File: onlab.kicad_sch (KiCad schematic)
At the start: 77 parts, among them J1 Battery, J10 DC-Motor, J2 HC_SR04, J3 HC_SR04, J4 HC_SR04, J5 DC-Motor, J6 DC-Motor, J7 DC-Motor, J8 DC-Motor, J9 DC-Motor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

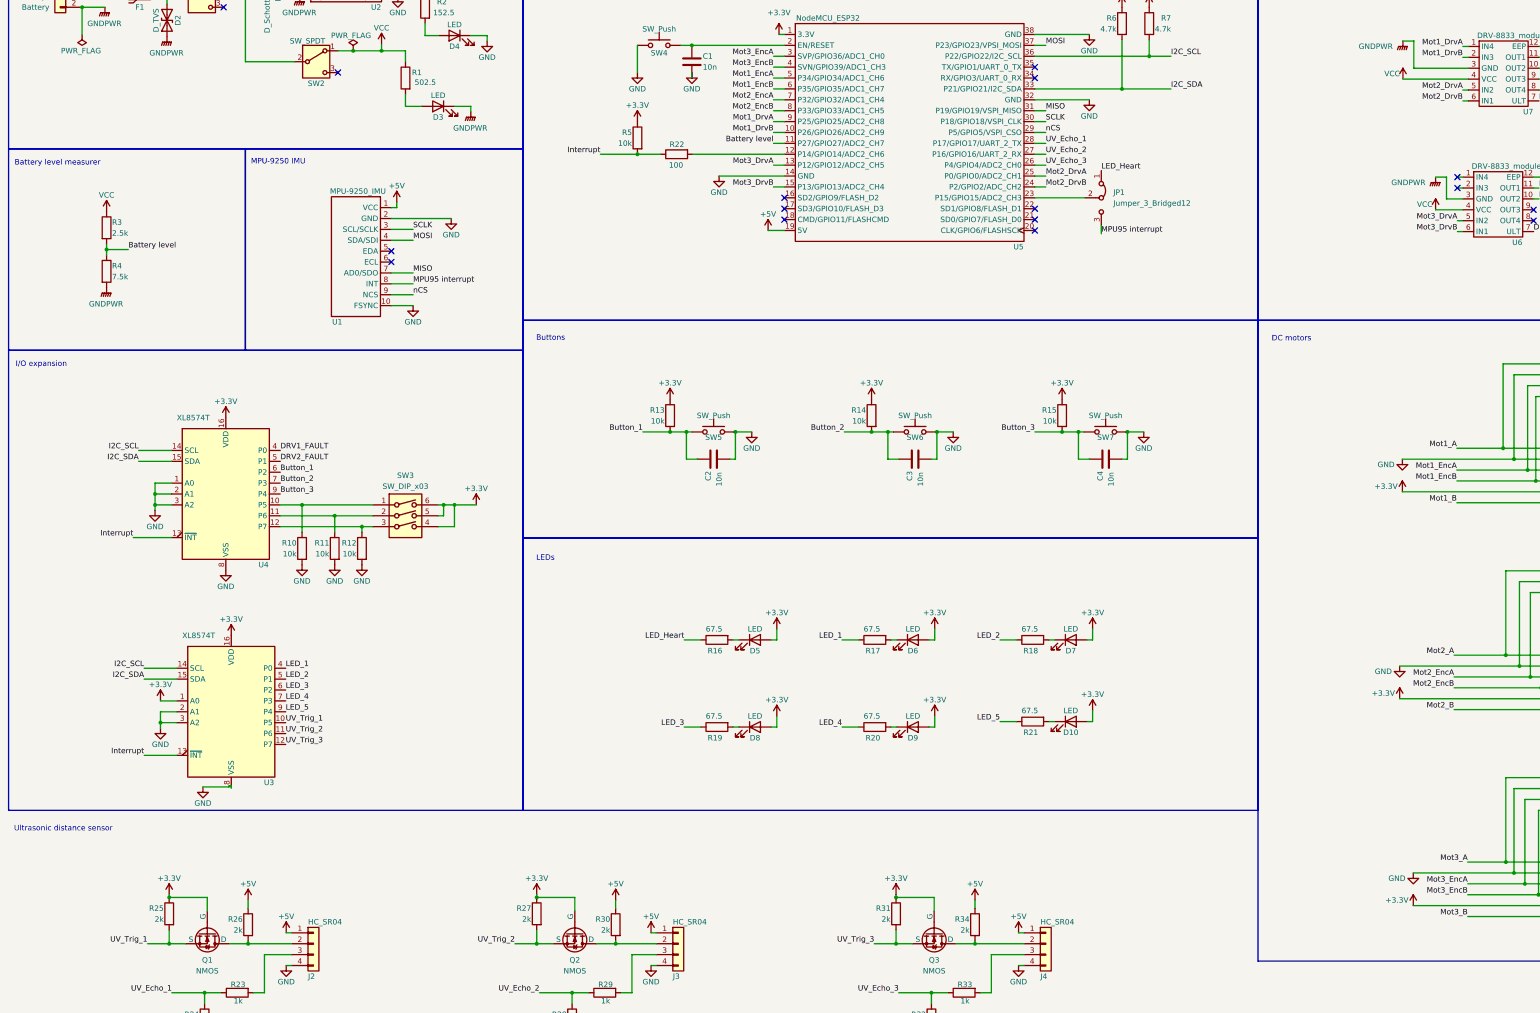
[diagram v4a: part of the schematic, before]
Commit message: schematic update
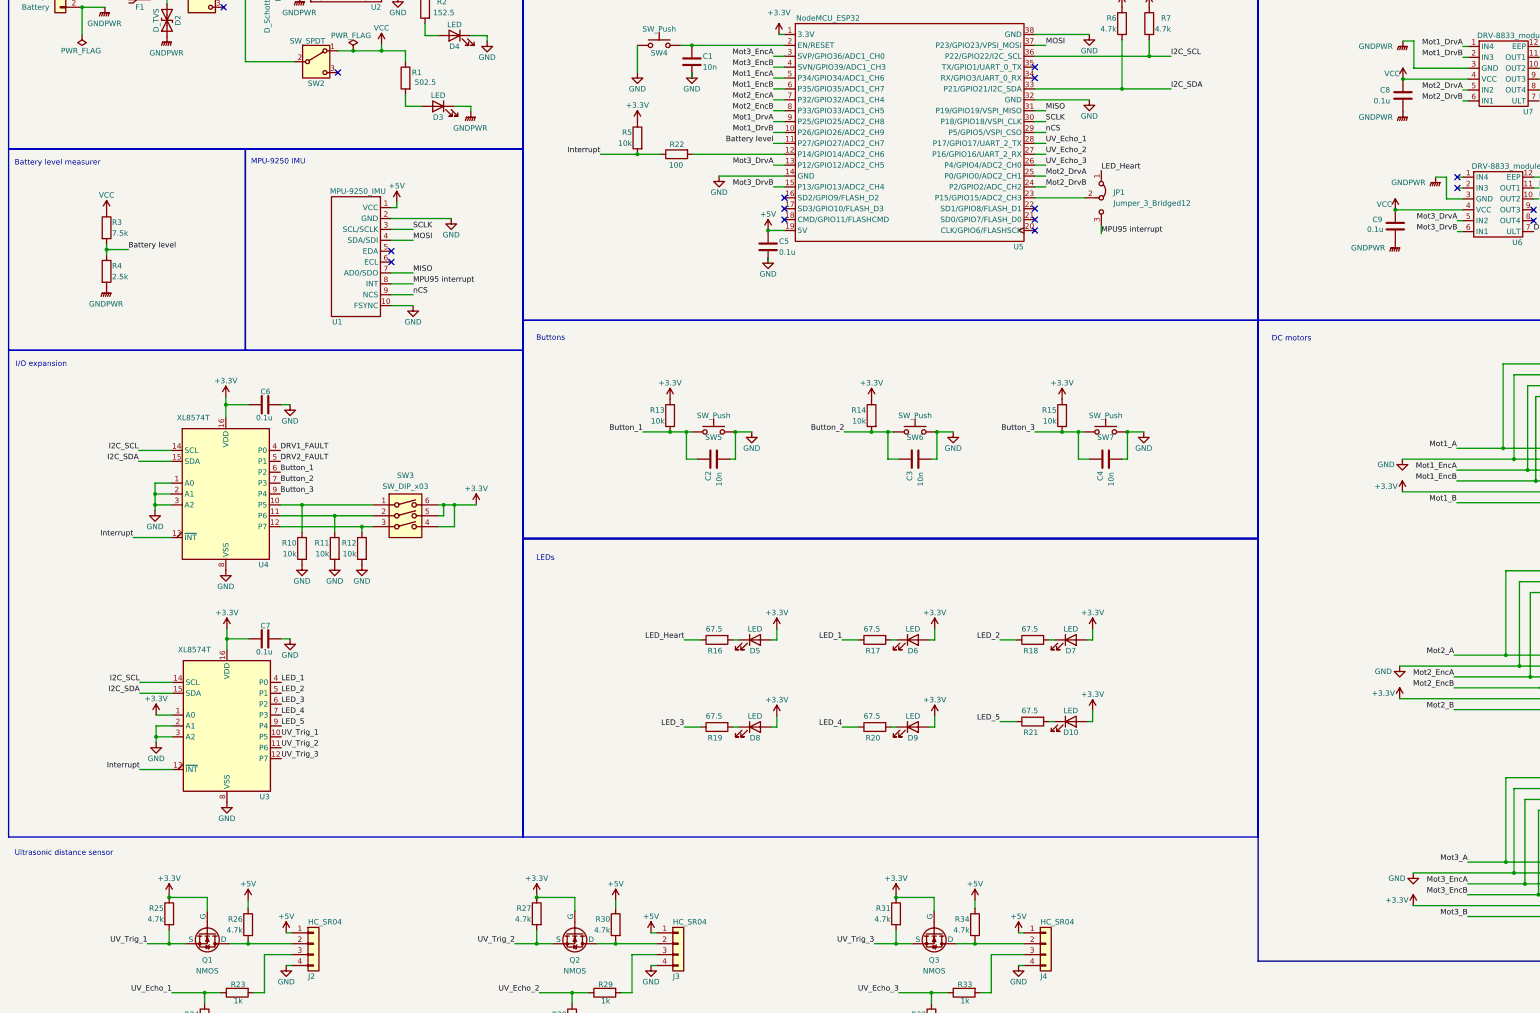
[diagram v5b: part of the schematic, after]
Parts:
- added C5, C6, C7, C8, C9: 0.1u, Capacitor_SMD:C_0805_2012Metric_Pad1.18x1.45mm_HandSolder, symbol Device:C
- R25, R26, R27, R30, R31, R34: value 2k -> 4.7k
- R3: value 2.5k -> 7.5k
- R4: value 7.5k -> 2.5k
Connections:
- net +3.3V: now also C6.1, C7.1
- net +5V: now also C5.1
- net GND: now also C5.2, C6.2, C7.2
- net GNDPWR: now also C8.2, C9.2
- net VCC: now also C8.1, C9.1
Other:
- moved on the sheet: U3

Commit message: footprint assignment final
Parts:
- JP1, SW1, SW2: footprint (none) -> Connector:FanPinHeader_1x03_P2.54mm_Vertical
- Q1, Q2, Q3: footprint (none) -> Package_TO_SOT_SMD:SOT-23_Handsoldering
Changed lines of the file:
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@@
   (title_block
     (title "Robot Schematic")
-    (date "2024-04-23")
-    (rev "v1.0")
+    (date "2024-05-25")
+    (rev "V6.0")
+    (comment 1 "Irányítás Technika Tanszék")
+    (comment 2 "Neptun: QVFLJH")
+    (comment 3 "Made by: Técsi Zsuzsanna Vilma")
   )
   (junction (at 361.315 181.61) (diameter 0) (color 0 0 0 0)
@@
       (effects (font (size 1.27 1.27)))
     )
-    (property "Footprint" "" (at 57.15 27.94 0)
+    (property "Footprint" "Connector:FanPinHeader_1x03_P2.54mm_Vertical" (at 57.15 27.94 0)
       (effects (font (size 1.27 1.27)) hide)
     )
@@
       (effects (font (size 1.27 1.27)))
     )
-    (property "Footprint" "" (at 230.505 251.46 0)
+    (property "Footprint" "Package_TO_SOT_SMD:SOT-23_Handsoldering" (at 230.505 251.46 0)
       (effects (font (size 1.27 1.27)) hide)
     )
@@
       (effects (font (size 1.27 1.27)))
     )
-    (property "Footprint" "" (at 60.96 251.46 0)
+    (property "Footprint" "Package_TO_SOT_SMD:SOT-23_Handsoldering" (at 60.96 251.46 0)
       (effects (font (size 1.27 1.27)) hide)
     )
@@
       (effects (font (size 1.27 1.27)) (justify left))
     )
-    (property "Footprint" "" (at 266.954 74.93 0)
+    (property "Footprint" "Connector:FanPinHeader_1x03_P2.54mm_Vertical" (at 266.954 74.93 0)
       (effects (font (size 1.27 1.27)) hide)
     )
@@
       (effects (font (size 1.27 1.27)))
     )
-    (property "Footprint" "" (at 83.82 43.18 0)
+    (property "Footprint" "Connector:FanPinHeader_1x03_P2.54mm_Vertical" (at 83.82 43.18 0)
       (effects (font (size 1.27 1.27)) hide)
     )
@@
       (effects (font (size 1.27 1.27)))
     )
-    (property "Footprint" "" (at 146.685 251.46 0)
+    (property "Footprint" "Package_TO_SOT_SMD:SOT-23_Handsoldering" (at 146.685 251.46 0)
       (effects (font (size 1.27 1.27)) hide)
     )

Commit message: motor footprint update
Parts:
- J10, J8, J9: footprint Connector_Molex:Molex_KK-254_AE-6410-06A_1x06_P2.54mm_Vertical -> Onlab:motor
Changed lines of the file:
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@@
     (stroke (width 0) (type default))
   )
+  (wire (pts (xy 266.954 67.31) (xy 266.954 68.58))
+    (stroke (width 0) (type default))
+  )
   (wire (pts (xy 104.648 40.64) (xy 99.06 40.64))
     (stroke (width 0) (type default))
@@
     (stroke (width 0) (type default))
   )
+  (wire (pts (xy 267.208 66.294) (xy 267.208 67.31))
+    (stroke (width 0) (type default))
+  )
   (wire (pts (xy 251.46 59.69) (xy 254 59.69))
     (stroke (width 0) (type default))
@@
     (stroke (width 0) (type default))
   )
+  (wire (pts (xy 369.57 82.804) (xy 367.792 82.804))
+    (stroke (width 0) (type default))
+  )
   (wire (pts (xy 50.038 141.478) (xy 46.228 141.478))
     (stroke (width 0) (type default))
@@
     (stroke (width 0) (type default))
   )
+  (wire (pts (xy 267.208 67.31) (xy 266.954 67.31))
+    (stroke (width 0) (type default))
+  )
   (wire (pts (xy 80.518 146.558) (xy 80.518 152.908))
     (stroke (width 0) (type default))
@@
     (stroke (width 0) (type default))
   )
+  (wire (pts (xy 371.602 52.324) (xy 369.062 52.324))
+    (stroke (width 0) (type default))
+  )
   (wire (pts (xy 254 62.23) (xy 251.46 62.23))
     (stroke (width 0) (type default))
@@
     (effects (font (size 1.27 1.27)) (justify left bottom))
   )
-  (label "DRV2_FAULT" (at 367.792 82.804 0) (fields_autoplaced)
+  (label "DRV2_FAULT" (at 369.57 82.804 0) (fields_autoplaced)
     (effects (font (size 1.27 1.27)) (justify left bottom))
   )
@@
     (effects (font (size 1.27 1.27)) (justify left bottom))
   )
-  (label "DRV1_FAULT" (at 369.062 52.324 0) (fields_autoplaced)
+  (label "DRV1_FAULT" (at 371.602 52.324 0) (fields_autoplaced)
     (effects (font (size 1.27 1.27)) (justify left bottom))
   )
@@
     (effects (font (size 1.27 1.27)) (justify right bottom))
   )
-  (label "LED_Heart" (at 266.954 68.58 0) (fields_autoplaced)
+  (label "LED_Heart" (at 267.208 66.294 0) (fields_autoplaced)
     (effects (font (size 1.27 1.27)) (justify left bottom))
   )
@@
     (effects (font (size 1.27 1.27)) (justify right bottom))
   )
+  (netclass_flag "" (length 2.54) (shape round) (at 258.318 74.93 180) (fields_autoplaced)
+    (effects (font (size 1.27 1.27)) (justify right bottom))
+    (property "Netclass" "signal" (at 259.0165 77.47 0)
+      (effects (font (size 1.27 1.27) italic) (justify left))
+    )
+  )
+  (netclass_flag "" (length 2.54) (shape round) (at 150.114 248.92 180) (fields_autoplaced)
+    (effects (font (size 1.27 1.27)) (justify right bottom))
+    (property "Netclass" "signal" (at 150.8125 251.46 0)
+      (effects (font (size 1.27 1.27) italic) (justify left))
+    )
+  )
+  (netclass_flag "" (length 2.54) (shape round) (at 255.27 178.054 0) (fields_autoplaced)
+    (effects (font (size 1.27 1.27)) (justify left bottom))
+    (property "Netclass" "signal" (at 255.9685 175.514 0)
+      (effects (font (size 1.27 1.27) italic) (justify left))
+    )
+  )
+  (netclass_flag "" (length 2.54) (shape round) (at 104.648 53.594 90) (fields_autoplaced)
+    (effects (font (size 1.27 1.27)) (justify left bottom))
+    (property "Netclass" "power" (at 102.108 52.8955 90)
+      (effects (font (size 1.27 1.27) italic) (justify left))
+    )
+  )
+  (netclass_flag "" (length 2.54) (shape round) (at 91.948 151.638 0) (fields_autoplaced)
+    (effects (font (size 1.27 1.27)) (justify left bottom))
+    (property "Netclass" "signal" (at 92.6465 149.098 0)
+      (effects (font (size 1.27 1.27) italic) (justify left))
+    )
+  )
+  (netclass_flag "" (length 2.54) (shape round) (at 71.374 260.35 180) (fields_autoplaced)
+    (effects (font (size 1.27 1.27)) (justify right bottom))
+    (property "Netclass" "signal" (at 72.0725 262.89 0)
+      (effects (font (size 1.27 1.27) italic) (justify left))
+    )
+  )
+  (netclass_flag "" (length 2.54) (shape round) (at 64.77 25.4 0) (fields_autoplaced)
+    (effects (font (size 1.27 1.27)) (justify left bottom))
+    (property "Netclass" "power" (at 65.4685 22.86 0)
+      (effects (font (size 1.27 1.27) italic) (justify left))
+    )
+  )
+  (netclass_flag "" (length 2.54) (shape round) (at 70.104 248.92 180) (fields_autoplaced)
+    (effects (font (size 1.27 1.27)) (justify right bottom))
+    (property "Netclass" "signal" (at 70.8025 251.46 0)
+      (effects (font (size 1.27 1.27) italic) (justify left))
+    )
+  )
+  (netclass_flag "" (length 2.54) (shape round) (at 218.44 178.054 0) (fields_autoplaced)
+    (effects (font (size 1.27 1.27)) (justify left bottom))
+    (property "Netclass" "signal" (at 219.1385 175.514 0)
+      (effects (font (size 1.27 1.27) italic) (justify left))
+    )
+  )
+  (netclass_flag "" (length 2.54) (shape round) (at 218.44 198.374 0) (fields_autoplaced)
+    (effects (font (size 1.27 1.27)) (justify left bottom))
+    (property "Netclass" "signal" (at 219.1385 195.834 0)
+      (effects (font (size 1.27 1.27) italic) (justify left))
+    )
+  )
+  (netclass_flag "" (length 2.54) (shape round) (at 181.864 178.054 0) (fields_autoplaced)
+    (effects (font (size 1.27 1.27)) (justify left bottom))
+    (property "Netclass" "signal" (at 182.5625 175.514 0)
+      (effects (font (size 1.27 1.27) italic) (justify left))
+    )
+  )
+  (netclass_flag "" (length 2.54) (shape round) (at 86.614 148.844 0) (fields_autoplaced)
+    (effects (font (size 1.27 1.27)) (justify left bottom))
+    (property "Netclass" "signal" (at 87.3125 146.304 0)
+      (effects (font (size 1.27 1.27) italic) (justify left))
+    )
+  )
+  (netclass_flag "" (length 2.54) (shape round) (at 109.22 37.084 180) (fields_autoplaced)
+    (effects (font (size 1.27 1.27)) (justify right bottom))
+    (property "Netclass" "power" (at 109.9185 39.624 0)
+      (effects (font (size 1.27 1.27) italic) (justify left))
+    )
+  )
+  (netclass_flag "" (length 2.54) (shape round) (at 173.482 64.77 0) (fields_autoplaced)
+    (effects (font (size 1.27 1.27)) (justify left bottom))
+    (property "Netclass" "signal" (at 174.1805 62.23 0)
+      (effects (font (size 1.27 1.27) italic) (justify left))
+    )
+  )
+  (netclass_flag "" (length 2.54) (shape round) (at 156.718 260.35 180) (fields_autoplaced)
+    (effects (font (size 1.27 1.27)) (justify right bottom))
+    (property "Netclass" "signal" (at 157.4165 262.89 0)
+      (effects (font (size 1.27 1.27) italic) (justify left))
+    )
+  )
+  (netclass_flag "" (length 2.54) (shape round) (at 84.074 146.558 0) (fields_autoplaced)
+    (effects (font (size 1.27 1.27)) (justify left bottom))
+    (property "Netclass" "signal" (at 84.7725 144.018 0)
+      (effects (font (size 1.27 1.27) italic) (justify left))
+    )
+  )
+  (netclass_flag "" (length 2.54) (shape round) (at 78.994 23.368 90) (fields_autoplaced)
+    (effects (font (size 1.27 1.27)) (justify left bottom))
+    (property "Netclass" "power" (at 76.454 22.6695 90)
+      (effects (font (size 1.27 1.27) italic) (justify left))
+    )
+  )
+  (netclass_flag "" (length 2.54) (shape round) (at 235.204 248.92 180) (fields_autoplaced)
+    (effects (font (size 1.27 1.27)) (justify right bottom))
+    (property "Netclass" "signal" (at 235.9025 251.46 0)
+      (effects (font (size 1.27 1.27) italic) (justify left))
+    )
+  )
+  (netclass_flag "" (length 2.54) (shape round) (at 255.27 197.104 0) (fields_autoplaced)
+    (effects (font (size 1.27 1.27)) (justify left bottom))
+    (property "Netclass" "signal" (at 255.9685 194.564 0)
+      (effects (font (size 1.27 1.27) italic) (justify left))
+    )
+  )
+  (netclass_flag "" (length 2.54) (shape round) (at 240.792 260.35 180) (fields_autoplaced)
+    (effects (font (size 1.27 1.27)) (justify right bottom))
+    (property "Netclass" "signal" (at 241.4905 262.89 0)
+      (effects (font (size 1.27 1.27) italic) (justify left))
+    )
+  )
+  (netclass_flag "" (length 2.54) (shape round) (at 50.292 27.94 0) (fields_autoplaced)
+    (effects (font (size 1.27 1.27)) (justify left bottom))
+    (property "Netclass" "power" (at 50.9905 25.4 0)
+      (effects (font (size 1.27 1.27) italic) (justify left))
+    )
+  )
+  (netclass_flag "" (length 2.54) (shape round) (at 181.61 198.374 0) (fields_autoplaced)
+    (effects (font (size 1.27 1.27)) (justify left bottom))
+    (property "Netclass" "signal" (at 182.3085 195.834 0)
+      (effects (font (size 1.27 1.27) italic) (justify left))
+    )
+  )
   (symbol (lib_id "power:VCC") (at 335.534 77.724 0) (unit 1)
     (in_bom yes) (on_board yes) (dnp no)
@@
       (effects (font (size 1.27 1.27)) (justify left))
     )
-    (property "Footprint" "Connector_Molex:Molex_KK-254_AE-6410-06A_1x06_P2.54mm_Vertical" (at 381.635 215.265 0)
+    (property "Footprint" "Onlab:motor" (at 381.635 215.265 0)
       (effects (font (size 1.27 1.27)) hide)
     )
@@
       (effects (font (size 1.27 1.27)) (justify left))
     )
-    (property "Footprint" "Connector_Molex:Molex_KK-254_AE-6410-06A_1x06_P2.54mm_Vertical" (at 381.635 118.745 0)
+    (property "Footprint" "Onlab:motor" (at 381.635 118.745 0)
       (effects (font (size 1.27 1.27)) hide)
     )
@@
       (effects (font (size 1.27 1.27)) (justify left))
     )
-    (property "Footprint" "Connector_Molex:Molex_KK-254_AE-6410-06A_1x06_P2.54mm_Vertical" (at 381.635 167.005 0)
+    (property "Footprint" "Onlab:motor" (at 381.635 167.005 0)
       (effects (font (size 1.27 1.27)) hide)
     )
